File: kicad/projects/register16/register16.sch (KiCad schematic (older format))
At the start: 35 parts

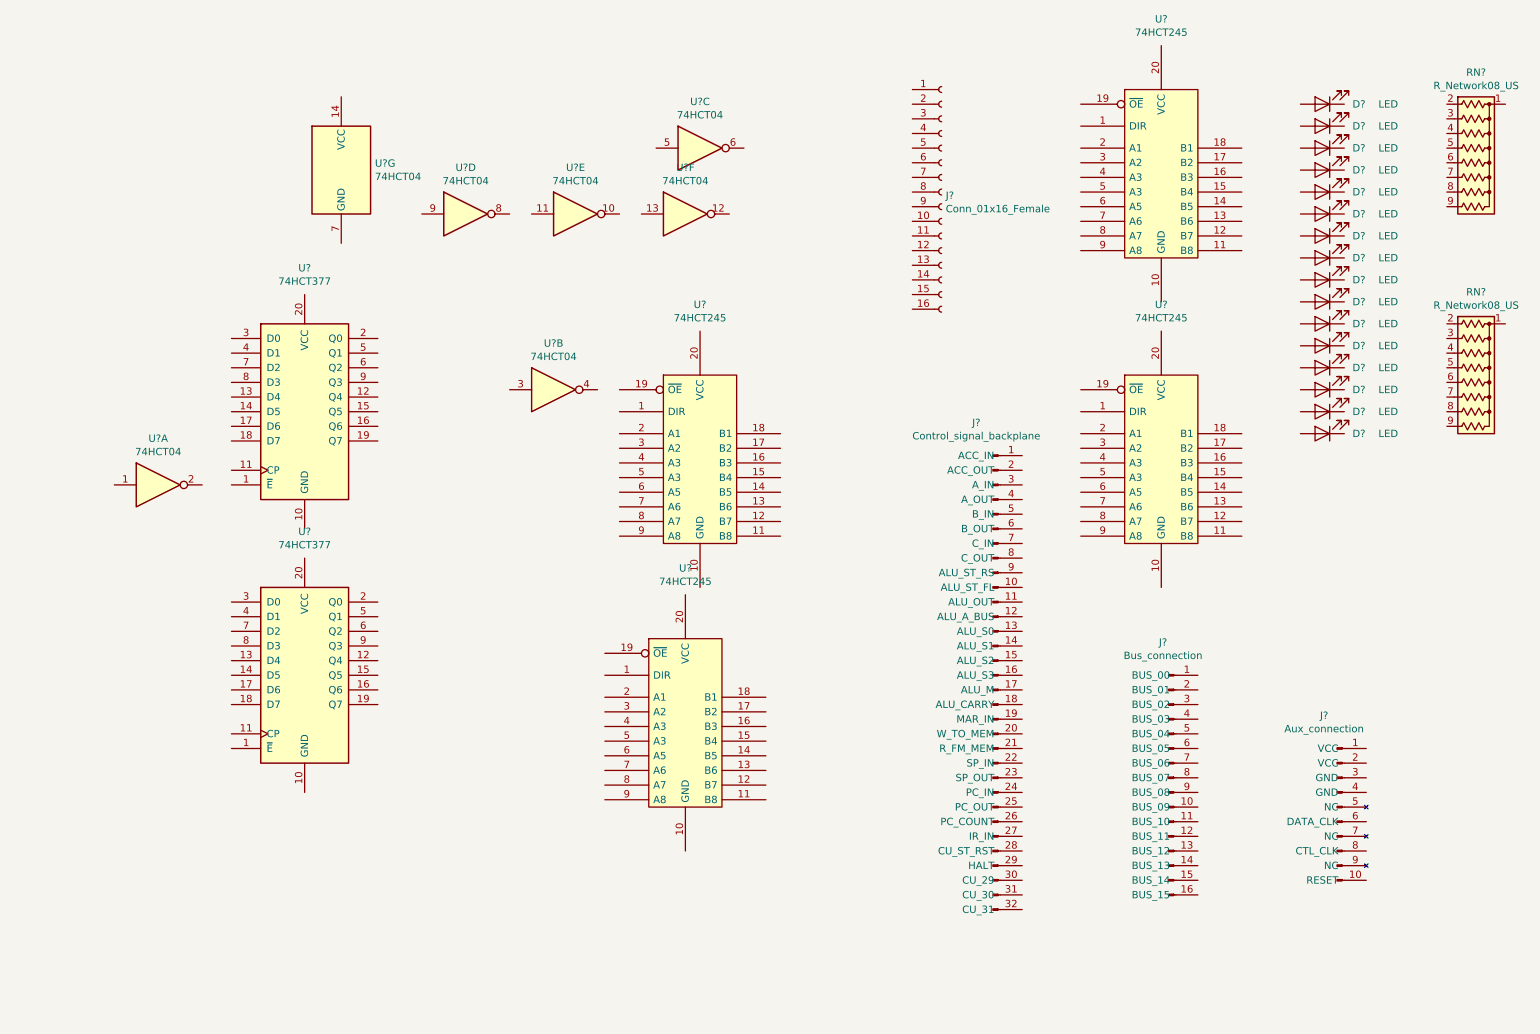
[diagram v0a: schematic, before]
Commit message: Finish register 16 schema placement and connection.
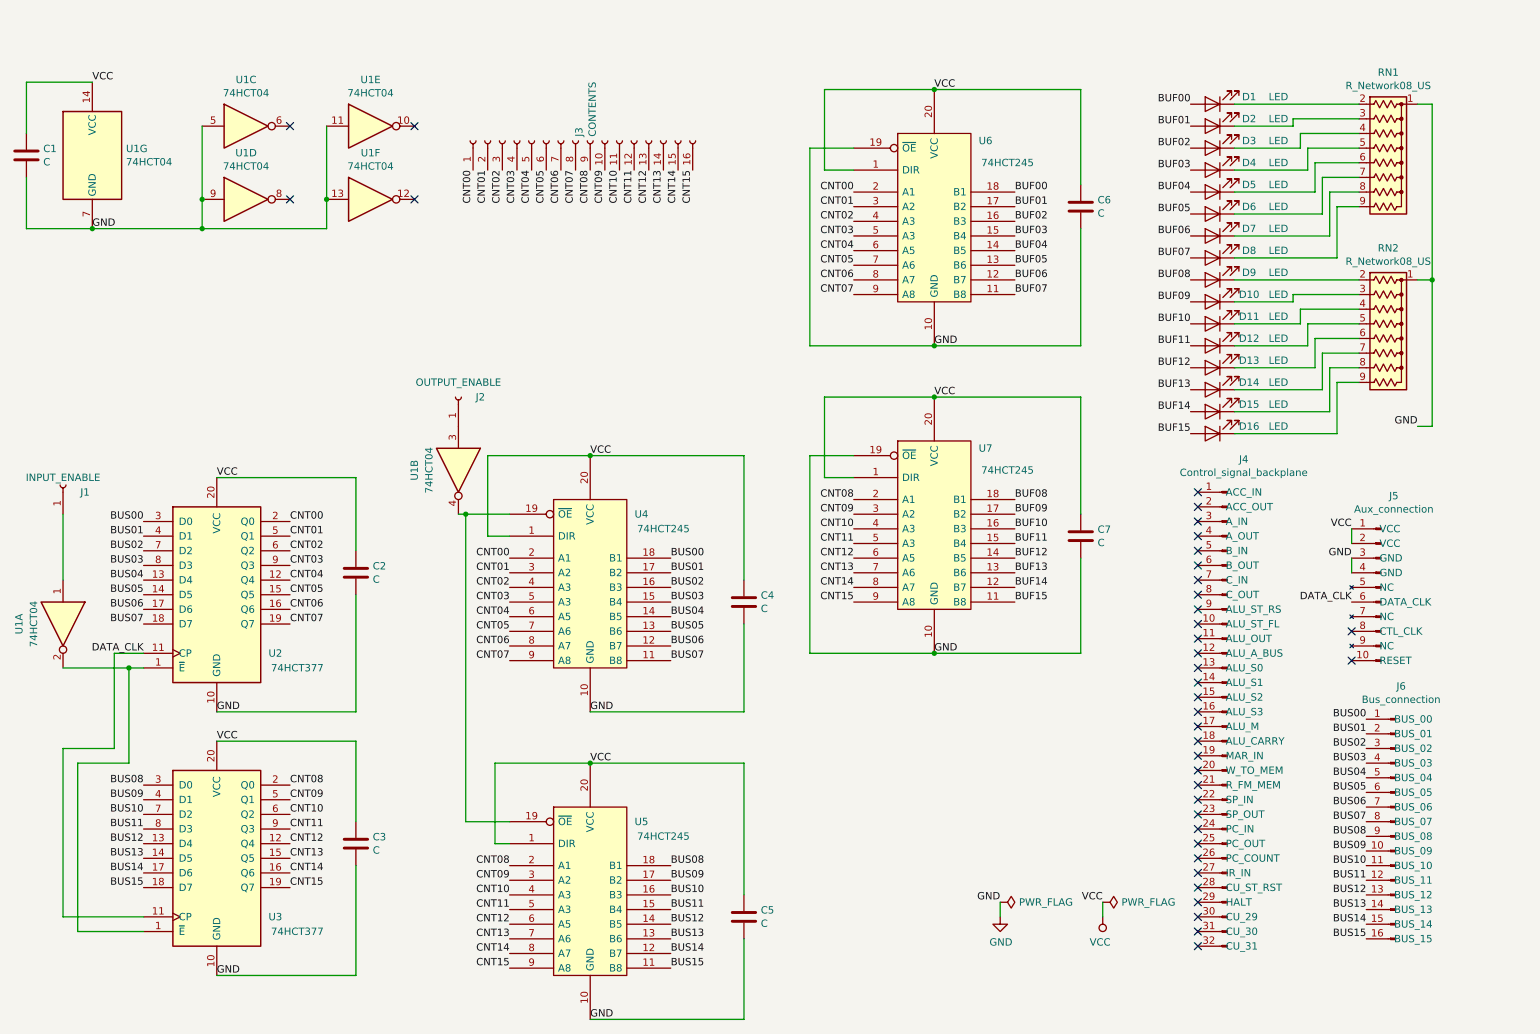
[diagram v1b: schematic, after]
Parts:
- removed D? (x12): LED, symbol Device:LED
- added C1, C2, C3, C4, C5, C6, C7: C, symbol Device:C
- added D10, D11, D12, D13, D14, D15, D16, D5, D6, D7, D8, D9: LED, symbol Device:LED
- added J1: INPUT_ENABLE, symbol Connector:Conn_01x01_Female
- added J2: OUTPUT_ENABLE, symbol Connector:Conn_01x01_Female
- J3: renamed from J?; value Conn_01x16_Female -> CONTENTS
- gave numbers to parts that had none: 16
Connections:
- net VCC: now reaches J5.1 (VCC)
- net VCC: now also J5.2 (VCC), U1.14 (VCC), U2.20 (VCC), U3.20 (VCC), U4.1 (DIR), U4.20 (VCC), U5.1 (DIR), U5.20 (VCC), U6.1 (DIR), U6.20 (VCC), U7.1 (DIR), U7.20 (VCC), C1.1, C2.1, C3.1, C4.1, C5.1, C6.1, C7.1
- net GND: now reaches J5.3 (GND)
- net GND: now also J5.4 (GND), RN1.1 (common), RN2.1 (common), U1.11, U1.13, U1.5, U1.7 (GND), U1.9, U2.10 (GND), U3.10 (GND), U4.10 (GND), U5.10 (GND), U6.10 (GND), U6.19 (~OE), U7.10 (GND), U7.19 (~OE), C1.2, C2.2, C3.2, C4.2, C5.2, C6.2, C7.2
- net DATA_CLK: now reaches J5.6 (DATA_CLK)
- net DATA_CLK: now also U2.11 (CP), U3.11 (CP)
- net BUS00: now reaches J6.1 (BUS_00)
- net BUS00: now also U2.3 (D0), U4.18 (B1)
- net BUS09: now reaches J6.10 (BUS_09)
- net BUS09: now also U3.4 (D1), U5.17 (B2)
- net BUS10: now reaches J6.11 (BUS_10)
- net BUS10: now also U3.7 (D2), U5.16 (B3)
- net BUS11: now reaches J6.12 (BUS_11)
- net BUS11: now also U3.8 (D3), U5.15 (B4)
- net BUS12: now reaches J6.13 (BUS_12)
- net BUS12: now also U3.13 (D4), U5.14 (B5)
- net BUS13: now reaches J6.14 (BUS_13)
- net BUS13: now also U3.14 (D5), U5.13 (B6)
- net BUS14: now reaches J6.15 (BUS_14)
- net BUS14: now also U3.17 (D6), U5.12 (B7)
- net BUS15: now reaches J6.16 (BUS_15)
- net BUS15: now also U3.18 (D7), U5.11 (B8)
- net BUS01: now reaches J6.2 (BUS_01)
- net BUS01: now also U2.4 (D1), U4.17 (B2)
- net BUS02: now reaches J6.3 (BUS_02)
- net BUS02: now also U2.7 (D2), U4.16 (B3)
- net BUS03: now reaches J6.4 (BUS_03)
- net BUS03: now also U2.8 (D3), U4.15 (B4)
- net BUS04: now reaches J6.5 (BUS_04)
- net BUS04: now also U2.13 (D4), U4.14 (B5)
- net BUS05: now reaches J6.6 (BUS_05)
- net BUS05: now also U2.14 (D5), U4.13 (B6)
- net BUS06: now reaches J6.7 (BUS_06)
- net BUS06: now also U2.17 (D6), U4.12 (B7)
- net BUS07: now reaches J6.8 (BUS_07)
- net BUS07: now also U2.18 (D7), U4.11 (B8)
- net BUS08: now reaches J6.9 (BUS_08)
- net BUS08: now also U3.3 (D0), U5.18 (B1)
- net at U4.19 (~OE): now also U1.4, U5.19 (~OE)
- net CNT00: now reaches U4.2 (A1)
- net CNT00: now also J3.1 (Pin_1), U2.2 (Q0), U6.2 (A1)
- net CNT01: now reaches U4.3 (A2)
- net CNT01: now also J3.2 (Pin_2), U2.5 (Q1), U6.3 (A2)
- net CNT02: now reaches U4.4 (A3)
- net CNT02: now also J3.3 (Pin_3), U2.6 (Q2), U6.4 (A3)
- net CNT03: now reaches U4.5 (A3)
- net CNT03: now also J3.4 (Pin_4), U2.9 (Q3), U6.5 (A3)
- net CNT04: now reaches U4.6 (A5)
- net CNT04: now also J3.5 (Pin_5), U2.12 (Q4), U6.6 (A5)
- net CNT05: now reaches U4.7 (A6)
- net CNT05: now also J3.6 (Pin_6), U2.15 (Q5), U6.7 (A6)
- net CNT06: now reaches U4.8 (A7)
- net CNT06: now also J3.7 (Pin_7), U2.16 (Q6), U6.8 (A7)
- net CNT07: now reaches U4.9 (A8)
- net CNT07: now also J3.8 (Pin_8), U2.19 (Q7), U6.9 (A8)
- net at U3.1 (~E): now also U1.2, U2.1 (~E)
- net CNT12: now reaches U3.12 (Q4)
- net CNT12: now also J3.13 (Pin_13), U5.6 (A5), U7.6 (A5)
- net CNT13: now reaches U3.15 (Q5)
- net CNT13: now also J3.14 (Pin_14), U5.7 (A6), U7.7 (A6)
- net CNT14: now reaches U3.16 (Q6)
- net CNT14: now also J3.15 (Pin_15), U5.8 (A7), U7.8 (A7)
- net CNT15: now reaches U3.19 (Q7)
- net CNT15: now also J3.16 (Pin_16), U5.9 (A8), U7.9 (A8)
- net CNT08: now reaches U3.2 (Q0)
- net CNT08: now also J3.9 (Pin_9), U5.2 (A1), U7.2 (A1)
- net CNT09: now reaches U3.5 (Q1)
- net CNT09: now also J3.10 (Pin_10), U5.3 (A2), U7.3 (A2)
- net CNT10: now reaches U3.6 (Q2)
- net CNT10: now also J3.11 (Pin_11), U5.4 (A3), U7.4 (A3)
- net CNT11: now reaches U3.9 (Q3)
- net CNT11: now also J3.12 (Pin_12), U5.5 (A3), U7.5 (A3)
- net at D2.1 (K): now also RN1.3 (R2)
- net BUF01: now reaches D2.2 (A)
- net BUF01: now also U6.17 (B2)
- net at RN1.2 (R1): now also D1.1 (K)
- net at RN1.4 (R3): now also D3.1 (K)
- net at RN1.5 (R4): now also D4.1 (K)
- net at RN1.6 (R5): now also D5.1 (K)
- net at RN1.7 (R6): now also D6.1 (K)
- net at RN1.8 (R7): now also D7.1 (K)
- net at RN1.9 (R8): now also D8.1 (K)
- net at RN2.2 (R1): now also D9.1 (K)
- net at RN2.3 (R2): now also D10.1 (K)
- net at RN2.4 (R3): now also D11.1 (K)
- net at RN2.5 (R4): now also D12.1 (K)
- net at RN2.6 (R5): now also D13.1 (K)
- net at RN2.7 (R6): now also D14.1 (K)
- net at RN2.8 (R7): now also D15.1 (K)
- net at RN2.9 (R8): now also D16.1 (K)
- net BUF00: now reaches D1.2 (A)
- net BUF00: now also U6.18 (B1)
- net BUF03: now reaches D4.2 (A)
- net BUF03: now also U6.15 (B4)
- net BUF02: now reaches D3.2 (A)
- net BUF02: now also U6.16 (B3)
- net at U1.1: now also J1.1 (Pin_1)
- net at U1.3: now also J2.1 (Pin_1)
- net BUF07: now reaches U6.11 (B8)
- net BUF07: now also D8.2 (A)
- net BUF06: now reaches U6.12 (B7)
- net BUF06: now also D7.2 (A)
- net BUF05: now reaches U6.13 (B6)
- net BUF05: now also D6.2 (A)
- net BUF04: now reaches U6.14 (B5)
- net BUF04: now also D5.2 (A)
- net BUF15: now reaches U7.11 (B8)
- net BUF15: now also D16.2 (A)
- net BUF14: now reaches U7.12 (B7)
- net BUF14: now also D15.2 (A)
- net BUF13: now reaches U7.13 (B6)
- net BUF13: now also D14.2 (A)
- net BUF12: now reaches U7.14 (B5)
- net BUF12: now also D13.2 (A)
- net BUF11: now reaches U7.15 (B4)
- net BUF11: now also D12.2 (A)
- net BUF10: now reaches U7.16 (B3)
- net BUF10: now also D11.2 (A)
- net BUF09: now reaches U7.17 (B2)
- net BUF09: now also D10.2 (A)
- net BUF08: now reaches U7.18 (B1)
- net BUF08: now also D9.2 (A)
- no-connect marks 0 -> 38
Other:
- moved on the sheet: D1, D2, D3, D4, J3, J4, J5, J6, RN1, RN2, U1A, U1B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

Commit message: Footprint association and initial component layout.
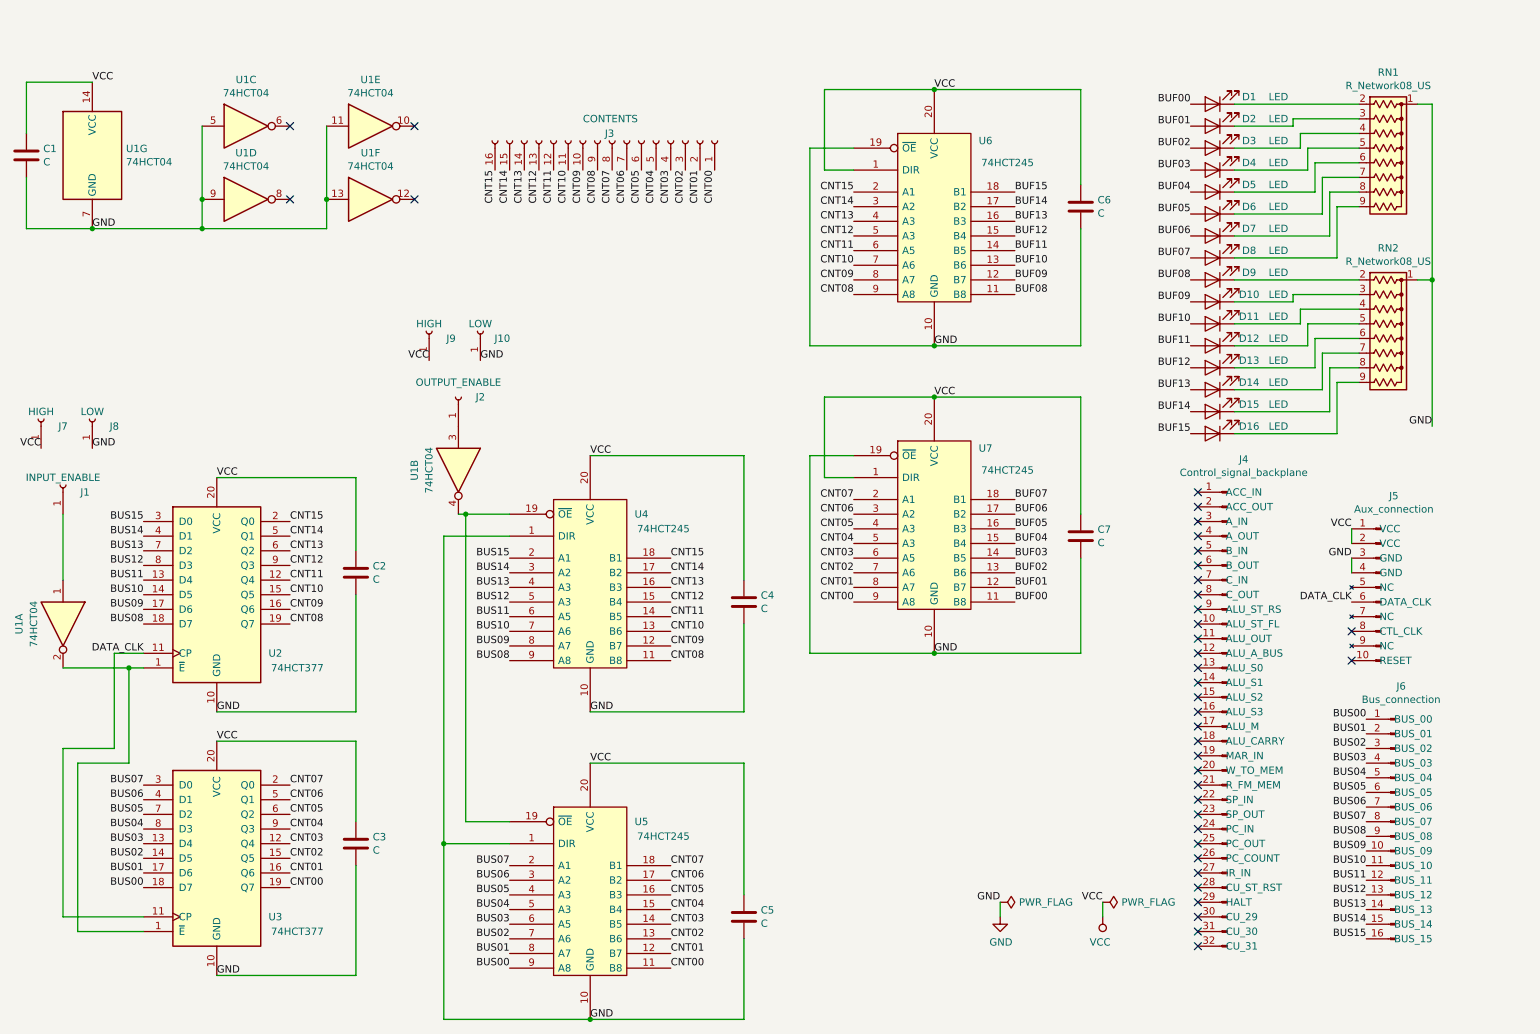
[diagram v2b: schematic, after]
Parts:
- added J10, J8: LOW, Connector_Wire:SolderWirePad_1x01_Drill1mm, symbol Connector:Conn_01x01_Female
- added J7, J9: HIGH, Connector_Wire:SolderWirePad_1x01_Drill1mm, symbol Connector:Conn_01x01_Female
- C1, C2, C3, C4, C5, C6, C7: footprint (none) -> Capacitor_THT:C_Disc_D4.3mm_W1.9mm_P5.00mm
- D1, D10, D11, D12, D13, D14, D15, D16, D2, D3, D4, D5, D6, D7, D8, D9: footprint (none) -> LED_THT:LED_D5.0mm_Horizontal_O3.81mm_Z3.0mm
- J1, J2: footprint (none) -> Connector_Wire:SolderWirePad_1x01_Drill1mm
- J3: footprint (none) -> Connector_PinSocket_2.54mm:PinSocket_1x16_P2.54mm_Horizontal
- J4: footprint (none) -> eight-bit-computer:backplane-connector
- J5: footprint (none) -> Connector_PinHeader_2.54mm:PinHeader_1x10_P2.54mm_Horizontal
- J6: footprint (none) -> Connector_PinHeader_2.54mm:PinHeader_1x16_P2.54mm_Horizontal
- U1: footprint (none) -> Package_DIP:DIP-14_W7.62mm_Socket
- U2, U3, U4, U5, U6, U7: footprint (none) -> Package_DIP:DIP-20_W7.62mm_Socket
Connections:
- net BUF00: now also U7.11 (B8); no longer U6.18 (B1)
- net BUF01: now also U7.12 (B7); no longer U6.17 (B2)
- net BUF02: now also U7.13 (B6); no longer U6.16 (B3)
- net BUF03: now also U7.14 (B5); no longer U6.15 (B4)
- net BUF04: now also U7.15 (B4); no longer U6.14 (B5)
- net BUF05: now also U7.16 (B3); no longer U6.13 (B6)
- net BUF06: now also U7.17 (B2); no longer U6.12 (B7)
- net BUF07: now also U7.18 (B1); no longer U6.11 (B8)
- net BUF08: now also U6.11 (B8); no longer U7.18 (B1)
- net BUF09: now also U6.12 (B7); no longer U7.17 (B2)
- net BUF10: now also U6.13 (B6); no longer U7.16 (B3)
- net BUF11: now also U6.14 (B5); no longer U7.15 (B4)
- net BUF12: now also U6.15 (B4); no longer U7.14 (B5)
- net BUF13: now also U6.16 (B3); no longer U7.13 (B6)
- net BUF14: now also U6.17 (B2); no longer U7.12 (B7)
- net BUF15: now also U6.18 (B1); no longer U7.11 (B8)
- net BUS00: now also U3.18 (D7), U5.9 (A8); no longer U2.3 (D0), U4.18 (B1)
- net BUS01: now also U3.17 (D6), U5.8 (A7); no longer U2.4 (D1), U4.17 (B2)
- net BUS02: now also U3.14 (D5), U5.7 (A6); no longer U2.7 (D2), U4.16 (B3)
- net BUS03: now also U3.13 (D4), U5.6 (A5); no longer U2.8 (D3), U4.15 (B4)
- net BUS04: now also U3.8 (D3), U5.5 (A3); no longer U2.13 (D4), U4.14 (B5)
- net BUS05: now also U3.7 (D2), U5.4 (A3); no longer U2.14 (D5), U4.13 (B6)
- net BUS06: now also U3.4 (D1), U5.3 (A2); no longer U2.17 (D6), U4.12 (B7)
- net BUS07: now also U3.3 (D0), U5.2 (A1); no longer U2.18 (D7), U4.11 (B8)
- net BUS08: now also U2.18 (D7), U4.9 (A8); no longer U3.3 (D0), U5.18 (B1)
- net BUS09: now also U2.17 (D6), U4.8 (A7); no longer U3.4 (D1), U5.17 (B2)
- net BUS10: now also U2.14 (D5), U4.7 (A6); no longer U3.7 (D2), U5.16 (B3)
- net BUS11: now also U2.13 (D4), U4.6 (A5); no longer U3.8 (D3), U5.15 (B4)
- net BUS12: now also U2.8 (D3), U4.5 (A3); no longer U3.13 (D4), U5.14 (B5)
- net BUS13: now also U2.7 (D2), U4.4 (A3); no longer U3.14 (D5), U5.13 (B6)
- net BUS14: now also U2.4 (D1), U4.3 (A2); no longer U3.17 (D6), U5.12 (B7)
- net BUS15: now also U2.3 (D0), U4.2 (A1); no longer U3.18 (D7), U5.11 (B8)
- net CNT00: now also U3.19 (Q7), U5.11 (B8), U7.9 (A8); no longer U2.2 (Q0), U4.2 (A1), U6.2 (A1)
- net CNT01: now also U3.16 (Q6), U5.12 (B7), U7.8 (A7); no longer U2.5 (Q1), U4.3 (A2), U6.3 (A2)
- net CNT02: now also U3.15 (Q5), U5.13 (B6), U7.7 (A6); no longer U2.6 (Q2), U4.4 (A3), U6.4 (A3)
- net CNT03: now also U3.12 (Q4), U5.14 (B5), U7.6 (A5); no longer U2.9 (Q3), U4.5 (A3), U6.5 (A3)
- net CNT04: now also U3.9 (Q3), U5.15 (B4), U7.5 (A3); no longer U2.12 (Q4), U4.6 (A5), U6.6 (A5)
- net CNT05: now also U3.6 (Q2), U5.16 (B3), U7.4 (A3); no longer U2.15 (Q5), U4.7 (A6), U6.7 (A6)
- net CNT06: now also U3.5 (Q1), U5.17 (B2), U7.3 (A2); no longer U2.16 (Q6), U4.8 (A7), U6.8 (A7)
- net CNT07: now also U3.2 (Q0), U5.18 (B1), U7.2 (A1); no longer U2.19 (Q7), U4.9 (A8), U6.9 (A8)
- net CNT08: now also U2.19 (Q7), U4.11 (B8), U6.9 (A8); no longer U3.2 (Q0), U5.2 (A1), U7.2 (A1)
- net CNT09: now also U2.16 (Q6), U4.12 (B7), U6.8 (A7); no longer U3.5 (Q1), U5.3 (A2), U7.3 (A2)
- net CNT10: now also U2.15 (Q5), U4.13 (B6), U6.7 (A6); no longer U3.6 (Q2), U5.4 (A3), U7.4 (A3)
- net CNT11: now also U2.12 (Q4), U4.14 (B5), U6.6 (A5); no longer U3.9 (Q3), U5.5 (A3), U7.5 (A3)
- net CNT12: now also U2.9 (Q3), U4.15 (B4), U6.5 (A3); no longer U3.12 (Q4), U5.6 (A5), U7.6 (A5)
- net CNT13: now also U2.6 (Q2), U4.16 (B3), U6.4 (A3); no longer U3.15 (Q5), U5.7 (A6), U7.7 (A6)
- net CNT14: now also U2.5 (Q1), U4.17 (B2), U6.3 (A2); no longer U3.16 (Q6), U5.8 (A7), U7.8 (A7)
- net CNT15: now also U2.2 (Q0), U4.18 (B1), U6.2 (A1); no longer U3.19 (Q7), U5.9 (A8), U7.9 (A8)
- net GND: now also U4.1 (DIR), U5.1 (DIR), J10.1 (Pin_1), J8.1 (Pin_1)
- net VCC: now also J7.1 (Pin_1), J9.1 (Pin_1); no longer U4.1 (DIR), U5.1 (DIR)
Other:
- moved on the sheet: J3
